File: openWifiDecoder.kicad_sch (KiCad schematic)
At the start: 63 parts, among them IC1 DRV8212DRLR, J1 Motor, J24 Hall, U1 MIC5317-1.8xM5, U2 MIC5219-3.3YM5, U3 ESP32-S3-MINI-1, U4 ICM-20948, U5 LTC4054ES5-4.2, U6 TL331, U7 BQ27441DRZT-G1A

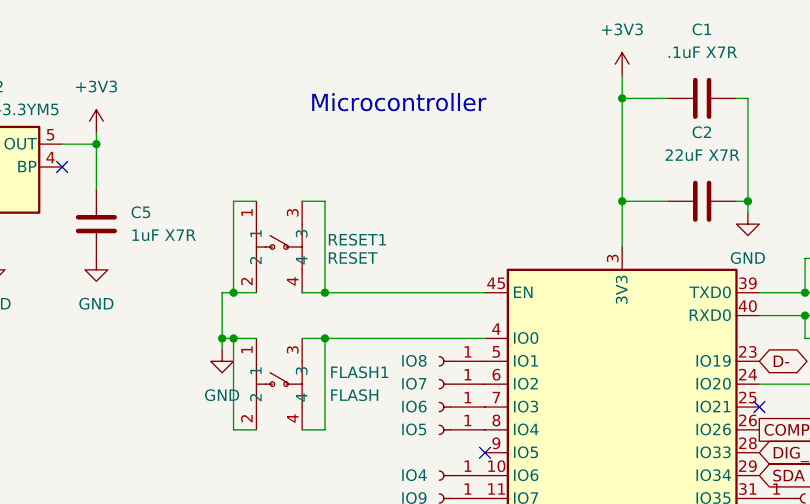
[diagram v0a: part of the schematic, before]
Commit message: add EN PullUp
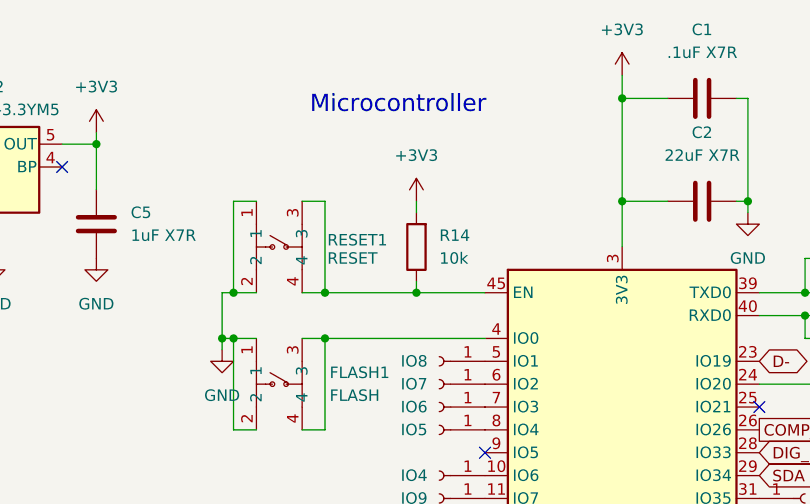
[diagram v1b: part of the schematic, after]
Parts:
- added R14: 10k, Resistor_SMD:R_0402_1005Metric, symbol Device:R
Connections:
- net +3V3: now also R14.2
- net at RESET1.3, RESET1.4, U3.45 (EN): now also R14.1
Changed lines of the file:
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@@
 	(generator_version "8.0")
 	(paper "A4")
+	(title_block
+		(rev "2")
+	)
 	(junction
 		(at 118.11 163.83)
@@
 	)
 	(junction
+		(at 121.92 43.18)
+		(diameter 0)
+		(color 0 0 0 0)
+	)
+	(junction
 		(at 41.91 71.12)
 		(diameter 0)
@@
 	(wire
 		(pts
+			(xy 121.92 43.18) (xy 129.54 43.18)
+		)
+		(stroke
+			(width 0)
+			(type default)
+		)
+	)
+	(wire
+		(pts
 			(xy 181.61 26.67) (xy 182.88 26.67)
 		)
@@
 	(wire
 		(pts
+			(xy 121.92 33.02) (xy 121.92 34.29)
+		)
+		(stroke
+			(width 0)
+			(type default)
+		)
+	)
+	(wire
+		(pts
 			(xy 165.1 45.72) (xy 160.02 45.72)
 		)
@@
 	(wire
 		(pts
+			(xy 121.92 41.91) (xy 121.92 43.18)
+		)
+		(stroke
+			(width 0)
+			(type default)
+		)
+	)
+	(wire
+		(pts
 			(xy 233.68 96.52) (xy 233.68 95.25)
 		)
@@
 	(wire
 		(pts
-			(xy 111.76 43.18) (xy 129.54 43.18)
+			(xy 111.76 43.18) (xy 121.92 43.18)
 		)
 		(stroke
@@
 	(symbol
 		(lib_id "power:+3V3")
+		(at 121.92 33.02 0)
+		(unit 1)
+		(exclude_from_sim no)
+		(in_bom yes)
+		(on_board yes)
+		(dnp no)
+		(fields_autoplaced yes)
+		(property "Reference" "#PWR052"
+			(at 121.92 36.83 0)
+			(effects
+				(font
+					(size 1.27 1.27)
+				)
+				(hide yes)
+			)
+		)
+		(property "Value" "+3V3"
+			(at 121.92 27.94 0)
+			(effects
+				(font
+					(size 1.27 1.27)
+				)
+			)
+		)
+		(property "Footprint" ""
+			(at 121.92 33.02 0)
+			(effects
+				(font
+					(size 1.27 1.27)
+				)
+				(hide yes)
+			)
+		)
+		(property "Datasheet" ""
+			(at 121.92 33.02 0)
+			(effects
+				(font
+					(size 1.27 1.27)
+				)
+				(hide yes)
+			)
+		)
+		(property "Description" "Power symbol creates a global label with name \"+3V3\""
+			(at 121.92 33.02 0)
+			(effects
+				(font
+					(size 1.27 1.27)
+				)
+				(hide yes)
+			)
+		)
+		(pin "1"
+		)
+		(instances
+			(project "openWifiDecoder"
+				(path "/bdf391a9-01cb-4cc3-af9a-dde3067524fd"
+					(reference "#PWR052")
+					(unit 1)
+				)
+			)
+		)
+	)
+	(symbol
+		(lib_id "power:+3V3")
 		(at 86.36 25.4 0)
 		(unit 1)
@@
 					(unit 1)
 				)
+			)
+		)
+	)
+	(symbol
+		(lib_id "Device:R")
+		(at 121.92 38.1 180)
+		(unit 1)
+		(exclude_from_sim no)
+		(in_bom yes)
+		(on_board yes)
+		(dnp no)
+		(fields_autoplaced yes)
+		(property "Reference" "R14"
+			(at 124.46 36.8299 0)
+			(effects
+				(font
+					(size 1.27 1.27)
+				)
+				(justify right)
+			)
+		)
+		(property "Value" "10k"
+			(at 124.46 39.3699 0)
+			(effects
+				(font
+					(size 1.27 1.27)
+				)
+				(justify right)
+			)
+		)
+		(property "Footprint" "Resistor_SMD:R_0402_1005Metric"
+			(at 123.698 38.1 90)
+			(effects
+				(font
+					(size 1.27 1.27)
+				)
+				(hide yes)
+			)
+		)
+		(property "Datasheet" "~"
+			(at 121.92 38.1 0)
+			(effects
+				(font
+					(size 1.27 1.27)
+				)
+				(hide yes)
+			)
+		)
+		(property "Description" "Resistor"
+			(at 121.92 38.1 0)
+			(effects
+				(font
+					(size 1.27 1.27)
+				)
+				(hide yes)
+			)
+		)
+		(pin "2"
+		)
+		(pin "1"
+		)
+		(instances
+			(project "openWifiDecoder"
+				(path "/bdf391a9-01cb-4cc3-af9a-dde3067524fd"
+					(reference "R14")
+					(unit 1)
+				)

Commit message: new KiCad version
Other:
- note added: "3.3V Regulator"
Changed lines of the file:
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@@
 (kicad_sch
-	(version 20231120)
+	(version 20250114)
 	(generator "eeschema")
-	(generator_version "8.0")
+	(generator_version "9.0")
 	(paper "A4")
 	(title_block
 		(rev "2")
 	)
+	(text "3.3V Regulator"
+		(exclude_from_sim no)
+		(at 75.184 17.018 0)
+		(effects
+			(font
+				(size 1.905 1.905)
+			)
+		)
+	)
+	(text "INTERRUPT"
+		(exclude_from_sim no)
+		(at 174.498 61.214 0)
+		(effects
+			(font
+				(size 1.016 1.016)
+			)
+		)
+	)
+	(text "Microcontroller"
+		(exclude_from_sim no)
+		(at 119.888 22.352 0)
+		(effects
+			(font
+				(size 1.905 1.905)
+			)
+		)
+	)
+	(text "IMU"
+		(exclude_from_sim no)
+		(at 44.704 62.23 0)
+		(effects
+			(font
+				(size 1.905 1.905)
+			)
+		)
+	)
+	(text "Trigger IMU"
+		(exclude_from_sim no)
+		(at 118.872 94.742 0)
+		(effects
+			(font
+				(size 1.016 1.016)
+			)
+		)
+	)
+	(text "Battery Charger"
+		(exclude_from_sim no)
+		(at 252.984 146.05 0)
+		(effects
+			(font
+				(size 1.905 1.905)
+			)
+		)
+	)
+	(text "Hall Effect\nComperator"
+		(exclude_from_sim no)
+		(at 61.468 153.416 0)
+		(effects
+			(font
+				(size 1.905 1.905)
+			)
+		)
+	)
+	(text "Motor Driver"
+		(exclude_from_sim no)
+		(at 225.806 28.956 0)
+		(effects
+			(font
+				(size 1.905 1.905)
+			)
+		)
+	)
+	(text "INTERRUPT"
+		(exclude_from_sim no)
+		(at 119.38 91.44 0)
+		(effects
+			(font
+				(size 1.016 1.016)
+			)
+		)
+	)
+	(text "USB-C Connector"
+		(exclude_from_sim no)
+		(at 140.716 144.272 0)
+		(effects
+			(font
+				(size 1.905 1.905)
+			)
+		)
+	)
+	(text "1.8V Regulator"
+		(exclude_from_sim no)
+		(at 44.45 17.018 0)
+		(effects
+			(font
+				(size 1.905 1.905)
+			)
+		)
+	)
+	(text "Battery Fuel Gauge"
+		(exclude_from_sim no)
+		(at 240.538 64.008 0)
+		(effects
+			(font
+				(size 1.905 1.905)
+			)
+		)
+	)
+	(text "PULLUP\nINTERRUPT"
+		(exclude_from_sim no)
+		(at 172.466 91.694 0)
+		(effects
+			(font
+				(size 1.016 1.016)
+			)
+		)
+	)
 	(junction
 		(at 118.11 163.83)
@@
 		)
 	)
-	(text "INTERRUPT"
-		(exclude_from_sim no)
-		(at 174.498 61.214 0)
-		(effects
-			(font
-				(size 1.016 1.016)
-			)
-		)
-	)
-	(text "Microcontroller"
-		(exclude_from_sim no)
-		(at 119.888 22.352 0)
-		(effects
-			(font
-				(size 1.905 1.905)
-			)
-		)
-	)
-	(text "IMU"
-		(exclude_from_sim no)
-		(at 44.704 62.23 0)
-		(effects
-			(font
-				(size 1.905 1.905)
-			)
-		)
-	)
-	(text "Trigger IMU"
-		(exclude_from_sim no)
-		(at 118.872 94.742 0)
-		(effects
-			(font
-				(size 1.016 1.016)
-			)
-		)
-	)
-	(text "Battery Charger"
-		(exclude_from_sim no)
-		(at 252.984 146.05 0)
-		(effects
-			(font
-				(size 1.905 1.905)
-			)
-		)
-	)
-	(text "Hall Effect\nComperator"
-		(exclude_from_sim no)
-		(at 61.468 153.416 0)
-		(effects
-			(font
-				(size 1.905 1.905)
-			)
-		)
-	)
-	(text "Motor Driver"
-		(exclude_from_sim no)
-		(at 225.806 28.956 0)
-		(effects
-			(font
-				(size 1.905 1.905)
-			)
-		)
-	)
-	(text "INTERRUPT"
-		(exclude_from_sim no)
-		(at 119.38 91.44 0)
-		(effects
-			(font
-				(size 1.016 1.016)
-			)
-		)
-	)
-	(text "USB-C Connector"
-		(exclude_from_sim no)
-		(at 140.716 144.272 0)
-		(effects
-			(font
-				(size 1.905 1.905)
-			)
-		)
-	)
-	(text "1.8V Regulator"
-		(exclude_from_sim no)
-		(at 44.45 17.018 0)
-		(effects
-			(font
-				(size 1.905 1.905)
-			)
-		)
-	)
-	(text "Battery Fuel Gauge"
-		(exclude_from_sim no)
-		(at 240.538 64.008 0)
-		(effects
-			(font
-				(size 1.905 1.905)
-			)
-		)
-	)
-	(text "PULLUP\nINTERRUPT"
-		(exclude_from_sim no)
-		(at 172.466 91.694 0)
-		(effects
-			(font
-				(size 1.016 1.016)
-			)
-		)
-	)
 	(global_label "DIG_HALL"
 		(shape input)
@@
 		)
 	)
+	(embedded_fonts no)
 )

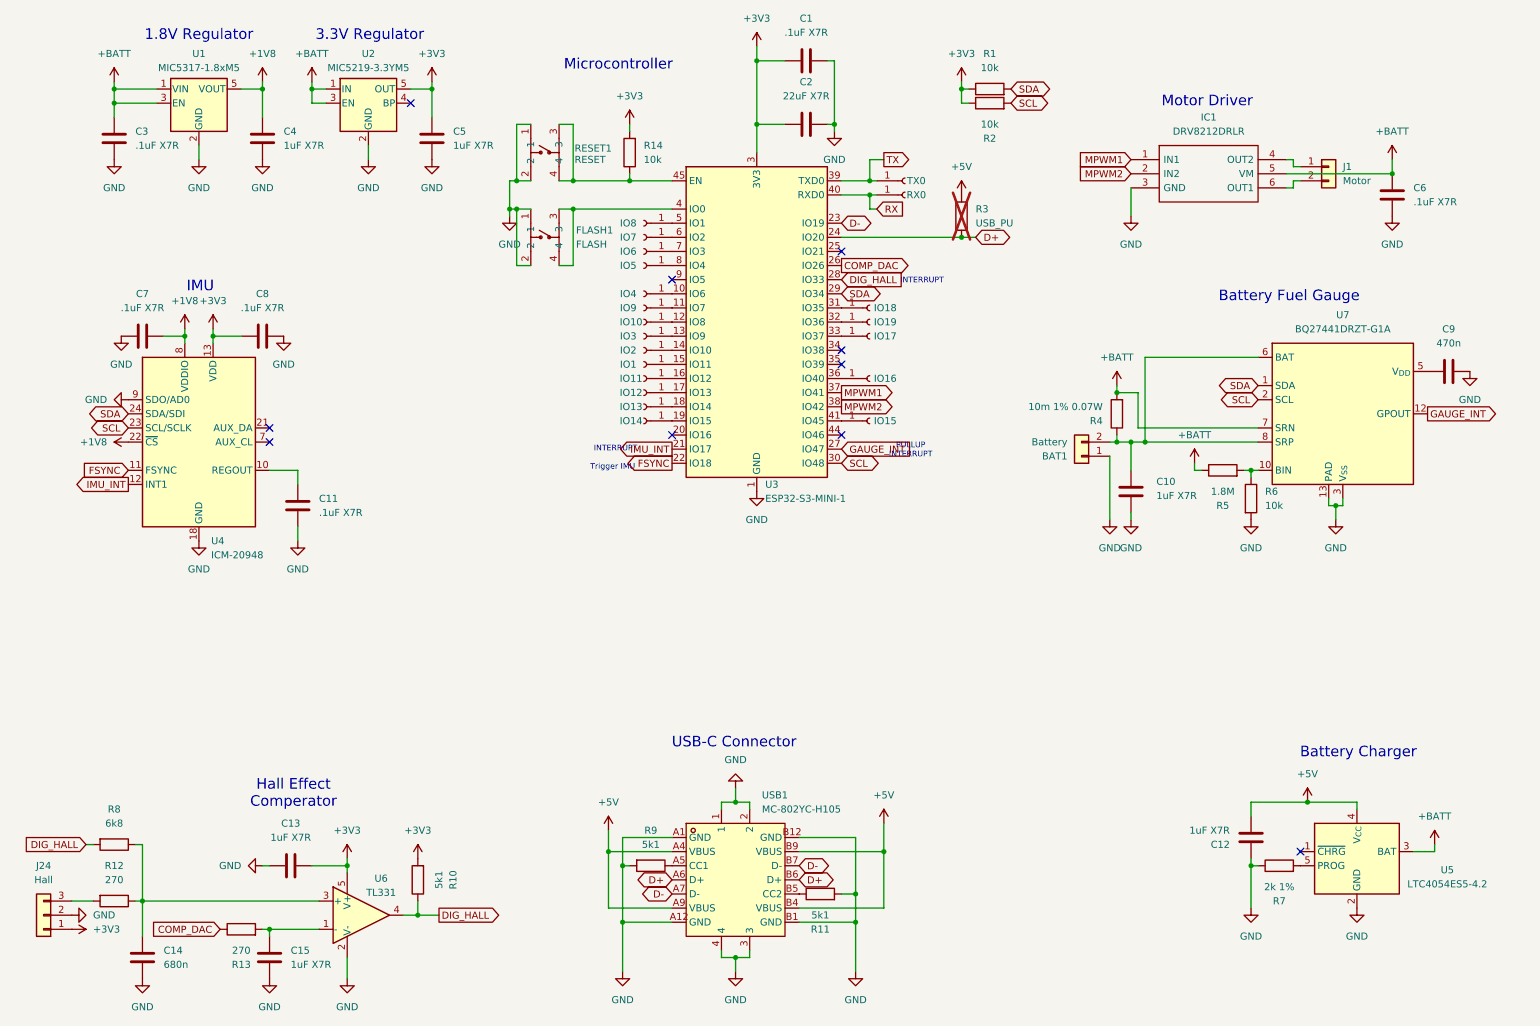
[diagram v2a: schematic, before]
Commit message: change LDO to Buck/Boost Converter in Schematic
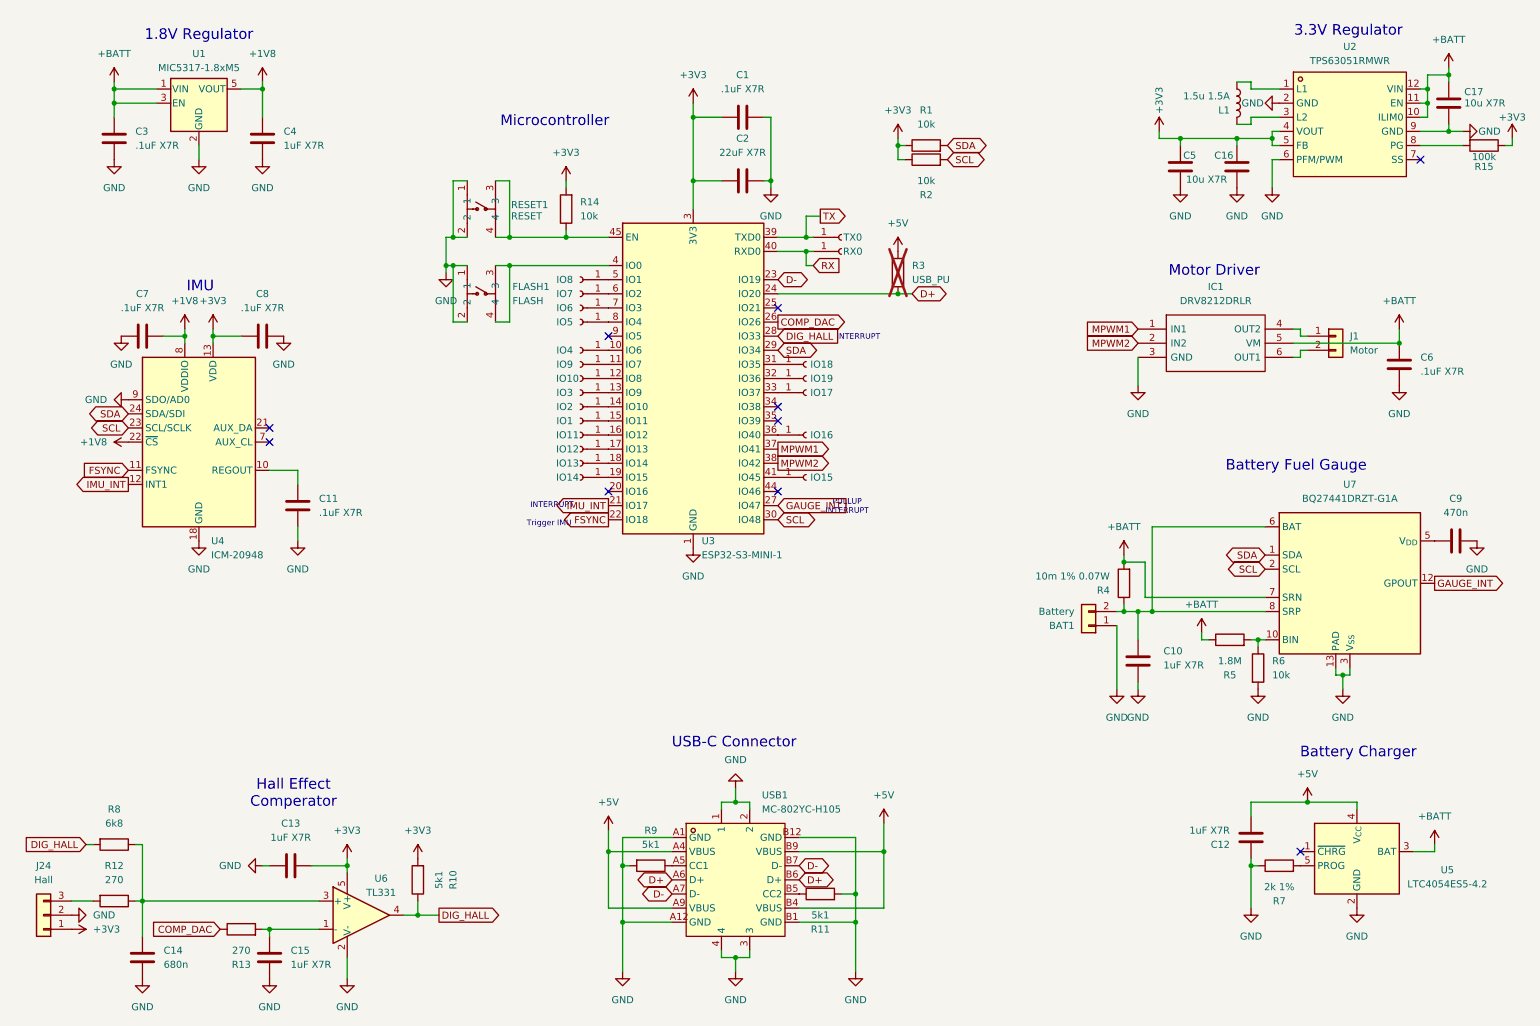
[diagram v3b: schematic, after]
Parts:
- removed U2: MIC5219-3.3YM5, Package_TO_SOT_SMD:SOT-23-5, symbol Regulator_Linear:MIC5219-3.3YM5
- added C16: 10u, Capacitor_SMD:C_0805_2012Metric, symbol Device:C
- added C17: 10u X7R, Capacitor_SMD:C_0805_2012Metric, symbol Device:C
- added L1: 1.5u 1.5A, Inductor_SMD:L_1008_2520Metric, symbol Device:L
- added R15: 100k, Resistor_SMD:R_0603_1608Metric, symbol Device:R
- added U2: TPS63051RMWR, EasyEDA:QFN-12_L2.5-W2.5-P0.50-TL, symbol EasyEda:TPS63051RMWR
- C5: value 1uF X7R -> 10u X7R; footprint Capacitor_SMD:C_0402_1005Metric -> Capacitor_SMD:C_0805_2012Metric
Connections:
- net +3V3: now also C16.1, R15.1, U2.4 (VOUT), U2.5 (FB)
- net +BATT: now also C17.1, U2.10 (ILIM0), U2.11 (EN), U2.12 (VIN)
- net GND: now also C16.2, C17.2, U2.2 (GND), U2.6 (PFM/PWM), U2.9 (GND)
- new net: L1.1, U2.1 (L1)
- new net: L1.2, U2.3 (L2)
- new net: R15.2, U2.8 (PG)
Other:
- moved on the sheet: BAT1, C1, C10, C2, C6, C9, FLASH1, IC1, IO1, IO10, IO11, IO12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
